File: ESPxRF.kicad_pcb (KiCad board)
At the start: 4 copper layers, 66.6 x 27.7 mm, 37 parts, among them J1 USB_C_Receptacle_USB2.0, J2 ANT, U1 NCP115ASN330T2G, U2 NRF24L01, U3 USBLC6-2SC6, U4 ESP32-S3, Y1 Crystal_GND24_Small

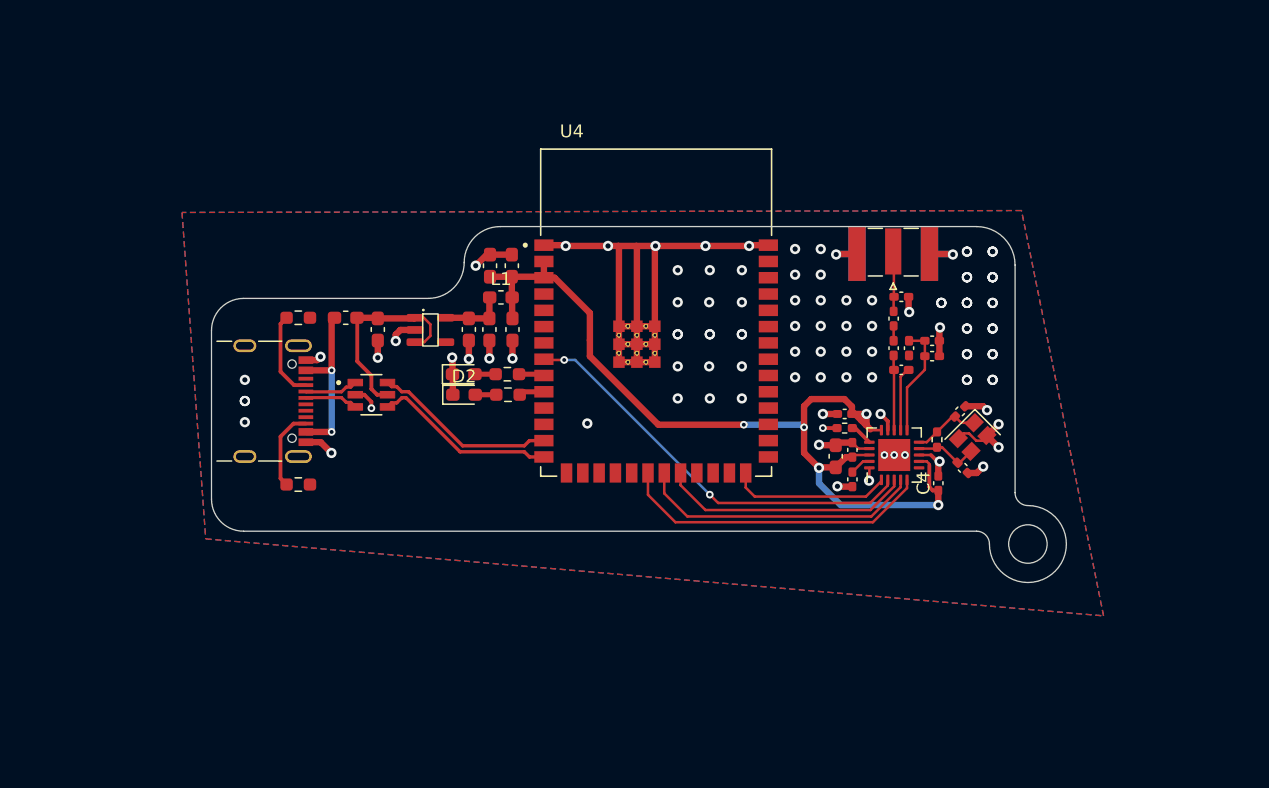
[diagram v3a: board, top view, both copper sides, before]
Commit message: made the ring sturdier and m2
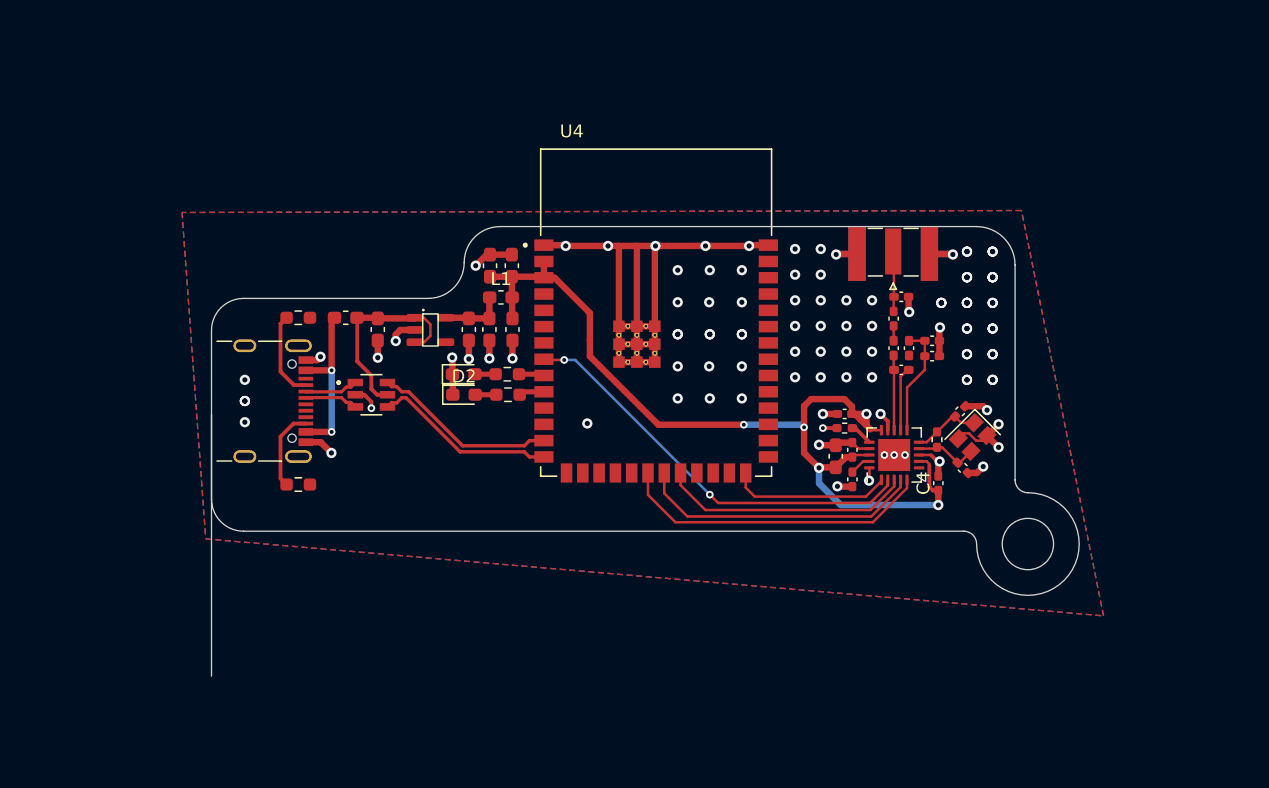
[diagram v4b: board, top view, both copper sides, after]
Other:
- board size 66.6 x 27.7 mm -> 67.6 x 35 mm
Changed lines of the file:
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@@
     )
   )
-  (gr_line (start 148.95 62.25) (end 148.95 80)
+  (gr_line (start 148.95 62.25) (end 148.95 79)
     (stroke (width 0.1) (type default)) (layer "Edge.Cuts"))
   (gr_arc (start 106 62.05) (mid 106.820101 60.070101) (end 108.8 59.25)
@@
   (gr_line (start 88.8 64.85) (end 103.2 64.85)
     (stroke (width 0.1) (type default)) (layer "Edge.Cuts"))
+  (gr_arc (start 144.95 83) (mid 145.657107 83.292893) (end 145.95 84)
+    (stroke (width 0.1) (type default)) (layer "Edge.Cuts"))
   (gr_arc (start 145.95 59.25) (mid 148.07132 60.12868) (end 148.95 62.25)
     (stroke (width 0.1) (type default)) (layer "Edge.Cuts"))
-  (gr_arc (start 145.95 83) (mid 146.657107 83.292893) (end 146.95 84)
-    (stroke (width 0.1) (type default)) (layer "Edge.Cuts"))
   (gr_line (start 108.8 59.25) (end 145.95 59.25)
     (stroke (width 0.1) (type default)) (layer "Edge.Cuts"))
-  (gr_circle (center 149.95 84) (end 151.45 84)
+  (gr_circle (center 149.95 84) (end 151.95 84)
     (stroke (width 0.1) (type default)) (fill none) (layer "Edge.Cuts"))
-  (gr_arc (start 149.95 81) (mid 152.07132 86.12132) (end 146.95 84)
-    (stroke (width 0.1) (type default)) (layer "Edge.Cuts"))
-  (gr_line (start 88.8 83) (end 145.95 83)
-    (stroke (width 0.1) (type default)) (layer "Edge.Cuts"))
-  (gr_arc (start 149.95 81) (mid 149.242893 80.707107) (end 148.95 80)
+  (gr_arc (start 149.95 80) (mid 152.778427 86.828427) (end 145.95 84)
+    (stroke (width 0.1) (type default)) (layer "Edge.Cuts"))
+  (gr_line (start 88.8 83) (end 144.95 83)
+    (stroke (width 0.1) (type default)) (layer "Edge.Cuts"))
+  (gr_arc (start 149.95 80) (mid 149.242893 79.707107) (end 148.95 79)
+    (stroke (width 0.1) (type default)) (layer "Edge.Cuts"))
+  (gr_line (start 86.3 73.925) (end 86.3 94.3)
     (stroke (width 0.1) (type default)) (layer "Edge.Cuts"))
   (gr_arc (start 88.8 83) (mid 87.032233 82.267767) (end 86.3 80.5)
@@
   (gr_text "RX" (at 102.165 71.56) (layer "F.Fab")
     (effects (font (size 1 1) (thickness 0.25) bold) (justify left bottom))
+  )
+  (dimension (type aligned) (layer "Edge.Cuts")
+    (pts (xy 86.3 84) (xy 153.95 84))
+    (height 7.999999)
+    (gr_text "67.6500 mm" (at 120.125 90.849999) (layer "Edge.Cuts")
+      (effects (font (size 1 1) (thickness 0.15)))
+    )
+    (format (prefix "") (suffix "") (units 3) (units_format 1) (precision 4))
+    (style (thickness 0.1) (arrow_length 1.27) (text_position_mode 0) (extension_height 0.58642) (extension_offset 0.5) keep_text_aligned)
+  )
+  (dimension (type aligned) (layer "Edge.Cuts")
+    (pts (xy 149.95 59.25) (xy 149.95 88))
+    (height -7.3)
+    (gr_text "28.7500 mm" (at 156.1 73.625 90) (layer "Edge.Cuts")
+      (effects (font (size 1 1) (thickness 0.15)))
+    )
+    (format (prefix "") (suffix "") (units 3) (units_format 1) (precision 4))
+    (style (thickness 0.1) (arrow_length 1.27) (text_position_mode 0) (extension_height 0.58642) (extension_offset 0.5) keep_text_aligned)
   )
   (segment (start 141.915 70.415946) (end 140.5275 71.803446) (width 0.2) (layer "F.Cu") (net 1))
@@
     (polygon
       (pts
-        (xy 152.95 84)
-        (xy 152.929715 83.651721)
-        (xy 152.869135 83.308152)
-        (xy 152.769078 82.97394)
-        (xy 152.630898 82.653602)
-        (xy 152.456463 82.351473)
-        (xy 152.248133 82.071637)
-        (xy 152.008725 81.817879)
-        (xy 151.741476 81.59363)
-        (xy 151.45 81.401924)
-        (xy 151.138239 81.245352)
-        (xy 150.81041 81.126031)
-        (xy 150.470945 81.045577)
-        (xy 150.124434 81.005076)
-        (xy 149.775566 81.005076)
-        (xy 149.429055 81.045577)
-        (xy 149.08959 81.126031)
-        (xy 148.761761 81.245352)
-        (xy 148.45 81.401924)
-        (xy 148.158524 81.59363)
-        (xy 147.891275 81.817879)
-        (xy 147.651867 82.071637)
-        (xy 147.443537 82.351473)
-        (xy 147.269102 82.653602)
-        (xy 147.130922 82.97394)
-        (xy 147.030865 83.308152)
-        (xy 146.970285 83.651721)
-        (xy 146.95 84)
-        (xy 146.970285 84.348279)
-        (xy 147.030865 84.691848)
-        (xy 147.130922 85.02606)
-        (xy 147.269102 85.346398)
-        (xy 147.443537 85.648527)
-        (xy 147.651867 85.928363)
-        (xy 147.891275 86.182121)
-        (xy 148.158524 86.40637)
-        (xy 148.45 86.598076)
-        (xy 148.761761 86.754648)
-        (xy 149.08959 86.873969)
-        (xy 149.429055 86.954423)
-        (xy 149.775566 86.994924)
-        (xy 150.124434 86.994924)
-        (xy 150.470945 86.954423)
-        (xy 150.81041 86.873969)
-        (xy 151.138239 86.754648)
-        (xy 151.45 86.598076)
-        (xy 151.741476 86.40637)
-        (xy 152.008725 86.182121)
-        (xy 152.248133 85.928363)
-        (xy 152.456463 85.648527)
-        (xy 152.630898 85.346398)
-        (xy 152.769078 85.02606)
-        (xy 152.869135 84.691848)
-        (xy 152.929715 84.348279)
-        (xy 152.95 84)
+        (xy 153.95 84)
+        (xy 153.930739 83.607931)
+        (xy 153.873141 83.219639)
+        (xy 153.777761 82.838861)
+        (xy 153.645518 82.469266)
+        (xy 153.477685 82.114413)
+        (xy 153.275878 81.777719)
+        (xy 153.042042 81.462427)
+        (xy 152.778427 81.171573)
+        (xy 152.487573 80.907958)
+        (xy 152.172281 80.674122)
+        (xy 151.835587 80.472315)
+        (xy 151.480734 80.304482)
+        (xy 151.111139 80.172239)
+        (xy 150.730361 80.076859)
+        (xy 150.342069 80.019261)
+        (xy 149.95 80)
+        (xy 149.557931 80.019261)
+        (xy 149.169639 80.076859)
+        (xy 148.788861 80.172239)
+        (xy 148.419266 80.304482)
+        (xy 148.064413 80.472315)
+        (xy 147.727719 80.674122)
+        (xy 147.412427 80.907958)
+        (xy 147.121573 81.171573)
+        (xy 146.857958 81.462427)
+        (xy 146.624122 81.777719)
+        (xy 146.422315 82.114413)
+        (xy 146.254482 82.469266)
+        (xy 146.122239 82.838861)
+        (xy 146.026859 83.219639)
+        (xy 145.969261 83.607931)
+        (xy 145.95 84)
+        (xy 145.969261 84.392069)
+        (xy 146.026859 84.780361)
+        (xy 146.122239 85.161139)
+        (xy 146.254482 85.530734)
+        (xy 146.422315 85.885587)
+        (xy 146.624122 86.222281)
+        (xy 146.857958 86.537573)
+        (xy 147.121573 86.828427)
+        (xy 147.412427 87.092042)
+        (xy 147.727719 87.325878)
+        (xy 148.064413 87.527685)
+        (xy 148.419266 87.695518)
+        (xy 148.788861 87.827761)
+        (xy 149.169639 87.923141)
+        (xy 149.557931 87.980739)
+        (xy 149.95 88)
+        (xy 150.342069 87.980739)
+        (xy 150.730361 87.923141)
+        (xy 151.111139 87.827761)
+        (xy 151.480734 87.695518)
+        (xy 151.835587 87.527685)
+        (xy 152.172281 87.325878)
+        (xy 152.487573 87.092042)
+        (xy 152.778427 86.828427)
+        (xy 153.042042 86.537573)
+        (xy 153.275878 86.222281)
+        (xy 153.477685 85.885587)
+        (xy 153.645518 85.530734)
+        (xy 153.777761 85.161139)
+        (xy 153.873141 84.780361)
+        (xy 153.930739 84.392069)
+        (xy 153.95 84)
       )
     )

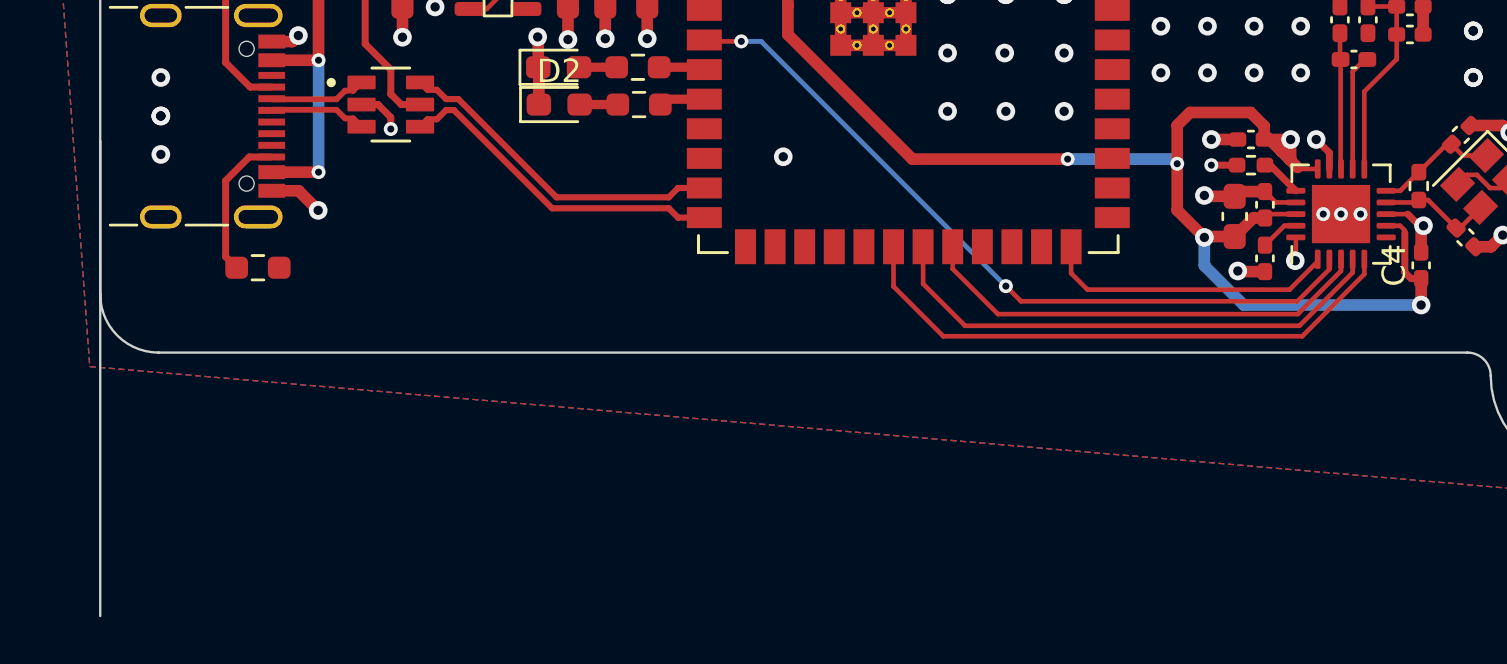
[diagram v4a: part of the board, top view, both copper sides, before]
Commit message: added pcb size measurements
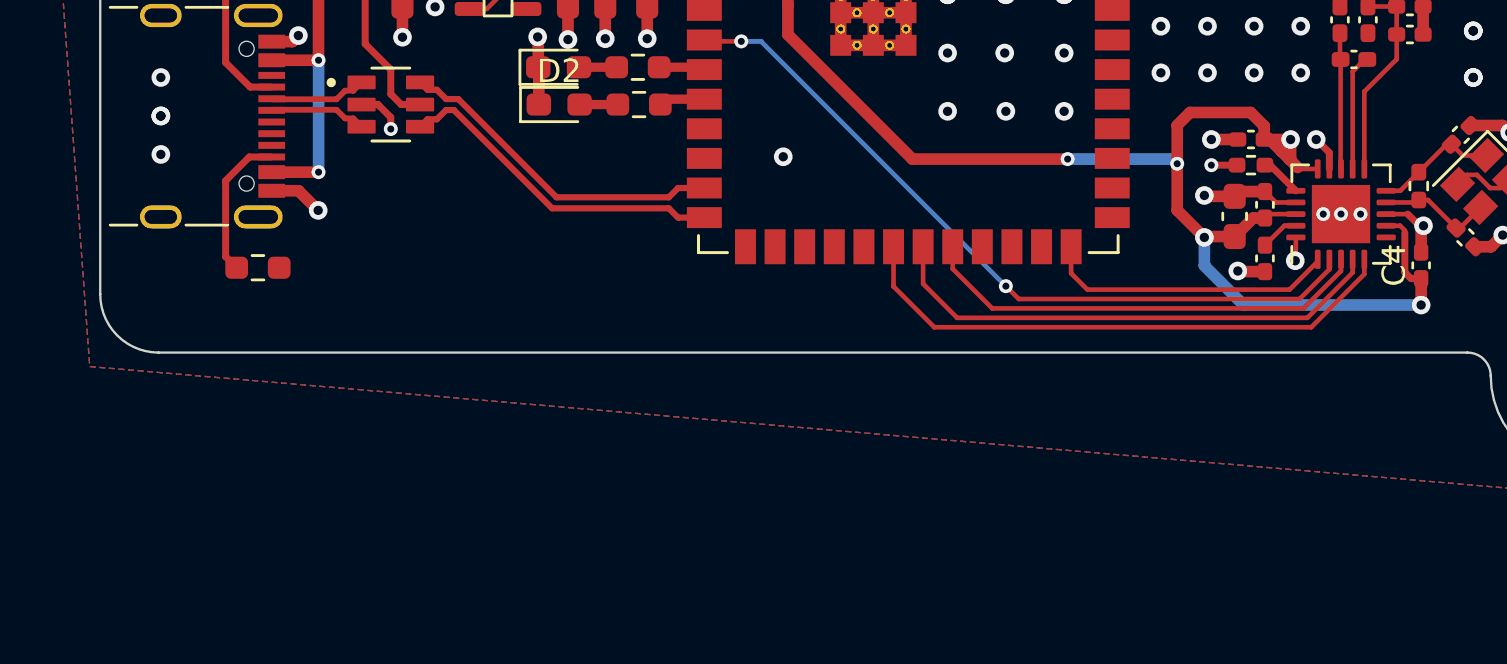
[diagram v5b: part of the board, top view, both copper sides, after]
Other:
- board size 67.6 x 35 mm -> 67.6 x 28.7 mm
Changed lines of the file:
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@@
   (gr_arc (start 149.95 80) (mid 149.242893 79.707107) (end 148.95 79)
-    (stroke (width 0.1) (type default)) (layer "Edge.Cuts"))
-  (gr_line (start 86.3 73.925) (end 86.3 94.3)
     (stroke (width 0.1) (type default)) (layer "Edge.Cuts"))
   (gr_arc (start 88.8 83) (mid 87.032233 82.267767) (end 86.3 80.5)
@@
   )
   (dimension (type aligned) (layer "Edge.Cuts")
-    (pts (xy 86.3 84) (xy 153.95 84))
-    (height 7.999999)
-    (gr_text "67.6500 mm" (at 120.125 90.849999) (layer "Edge.Cuts")
+    (pts (xy 149.95 59.25) (xy 149.95 88))
+    (height -7.7)
+    (gr_text "28.7500 mm" (at 156.5 73.625 90) (layer "Edge.Cuts")
       (effects (font (size 1 1) (thickness 0.15)))
     )
@@
   )
   (dimension (type aligned) (layer "Edge.Cuts")
-    (pts (xy 149.95 59.25) (xy 149.95 88))
-    (height -7.3)
-    (gr_text "28.7500 mm" (at 156.1 73.625 90) (layer "Edge.Cuts")
+    (pts (xy 86.3 84) (xy 153.95 84))
+    (height 7.999999)
+    (gr_text "67.6500 mm" (at 120.125 90.849999) (layer "Edge.Cuts")
       (effects (font (size 1 1) (thickness 0.15)))
     )
@@
   (segment (start 138.5275 78.9975) (end 138.5275 79.091975) (width 0.2) (layer "F.Cu") (net 9))
   (segment (start 128.65 80.3) (end 127.95 79.6) (width 0.2) (layer "F.Cu") (net 9))
+  (segment (start 137.751478 80.7032) (end 125.7032 80.7032) (width 0.2) (layer "F.Cu") (net 10))
+  (segment (start 112.275 69.65) (end 112.215 69.59) (width 0.2) (layer "F.Cu") (net 10))
+  (segment (start 139.0275 79.427178) (end 137.751478 80.7032) (width 0.2) (layer "F.Cu") (net 10))
+  (segment (start 125.7032 80.7032) (end 125.15 80.15) (width 0.2) (layer "F.Cu") (net 10))
+  (segment (start 113.8 69.65) (end 112.275 69.65) (width 0.2) (layer "F.Cu") (net 10))
   (segment (start 139.0275 78.9975) (end 139.0275 79.427178) (width 0.2) (layer "F.Cu") (net 10))
-  (segment (start 112.275 69.65) (end 112.215 69.59) (width 0.2) (layer "F.Cu") (net 10))
-  (segment (start 139.0275 79.427178) (end 137.654678 80.8) (width 0.2) (layer "F.Cu") (net 10))
-  (segment (start 125.8 80.8) (end 125.15 80.15) (width 0.2) (layer "F.Cu") (net 10))
-  (segment (start 113.8 69.65) (end 112.275 69.65) (width 0.2) (layer "F.Cu") (net 10))
-  (segment (start 137.654678 80.8) (end 125.8 80.8) (width 0.2) (layer "F.Cu") (net 10))
   (via (at 125.15 80.15) (size 0.6) (drill 0.3) (layers "F.Cu" "B.Cu") (net 10))
   (via (at 113.8 69.65) (size 0.6) (drill 0.3) (layers "F.Cu" "B.Cu") (net 10))
   (segment (start 114.65 69.65) (end 113.8 69.65) (width 0.2) (layer "B.Cu") (net 10))
   (segment (start 125.15 80.15) (end 114.65 69.65) (width 0.2) (layer "B.Cu") (net 10))
-  (segment (start 137.674888 81.35) (end 124.81 81.35) (width 0.2) (layer "F.Cu") (net 11))
+  (segment (start 122.87 79.41) (end 122.87 78.46) (width 0.2) (layer "F.Cu") (net 11))
   (segment (start 139.5275 78.9975) (end 139.5275 79.497388) (width 0.2) (layer "F.Cu") (net 11))
-  (segment (start 139.5275 79.497388) (end 137.674888 81.35) (width 0.2) (layer "F.Cu") (net 11))
-  (segment (start 124.81 81.35) (end 122.87 79.41) (width 0.2) (layer "F.Cu") (net 11))
-  (segment (start 122.87 79.41) (end 122.87 78.46) (width 0.2) (layer "F.Cu") (net 11))
-  (segment (start 140.0275 79.567598) (end 137.745098 81.85) (width 0.2) (layer "F.Cu") (net 12))
-  (segment (start 123.4 81.85) (end 121.6 80.05) (width 0.2) (layer "F.Cu") (net 12))
+  (segment (start 124.5664 81.1064) (end 122.87 79.41) (width 0.2) (layer "F.Cu") (net 11))
+  (segment (start 137.918488 81.1064) (end 124.5664 81.1064) (width 0.2) (layer "F.Cu") (net 11))
+  (segment (start 139.5275 79.497388) (end 137.918488 81.1064) (width 0.2) (layer "F.Cu") (net 11))
   (segment (start 140.0275 78.9975) (end 140.0275 79.567598) (width 0.2) (layer "F.Cu") (net 12))
-  (segment (start 137.745098 81.85) (end 123.4 81.85) (width 0.2) (layer "F.Cu") (net 12))
+  (segment (start 138.085498 81.5096) (end 123.0596 81.5096) (width 0.2) (layer "F.Cu") (net 12))
+  (segment (start 123.0596 81.5096) (end 121.6 80.05) (width 0.2) (layer "F.Cu") (net 12))
+  (segment (start 140.0275 79.567598) (end 138.085498 81.5096) (width 0.2) (layer "F.Cu") (net 12))
   (segment (start 121.6 80.05) (end 121.6 78.46) (width 0.2) (layer "F.Cu") (net 12))
+  (segment (start 138.252508 81.9128) (end 122.07939 81.9128) (width 0.2) (layer "F.Cu") (net 13))
   (segment (start 120.33 80.16341) (end 120.33 78.46) (width 0.2) (layer "F.Cu") (net 13))
-  (segment (start 122.46659 82.3) (end 120.33 80.16341) (width 0.2) (layer "F.Cu") (net 13))
+  (segment (start 122.07939 81.9128) (end 120.33 80.16341) (width 0.2) (layer "F.Cu") (net 13))
+  (segment (start 140.5275 79.637808) (end 138.252508 81.9128) (width 0.2) (layer "F.Cu") (net 13))
   (segment (start 140.5275 78.9975) (end 140.5275 79.637808) (width 0.2) (layer "F.Cu") (net 13))
-  (segment (start 140.5275 79.637808) (end 137.865308 82.3) (width 0.2) (layer "F.Cu") (net 13))
-  (segment (start 137.865308 82.3) (end 122.46659 82.3) (width 0.2) (layer "F.Cu") (net 13))
   (segment (start 107.965 66.3725) (end 107.965 64.7975) (width 0.5) (layer "F.Cu") (net 15))
   (segment (start 107.915 66.3225) (end 107.965 66.3725) (width 0.5) (layer "F.Cu") (net 15))

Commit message: added GND plane in two inner layers
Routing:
- added copper zone on In1.Cu, net GND
- added copper zone on In2.Cu, net GND
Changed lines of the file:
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@@
     (pad "6" smd roundrect (at 1.255 -0.95) (size 1.21 0.59) (layers "F.Cu" "F.Paste" "F.Mask") (roundrect_rratio 0.07)
       (net 34 "USB_D-") (pintype "bidirectional"))
-    (model "C:/Program Files/KiCad/6.0/share/kicad/3dmodels/Diode_SMD.3dshapes/USBLC6-2SC6.STEP"
+    (model "${KIPRJMOD}/KicadLibs/USBLC6-2SC6/USBLC6-2SC6.STEP"
       (offset (xyz 0 0 1))
       (scale (xyz 1 1 1))
@@
     (pad "2" smd rect (at 2.825 0 180) (size 1.35 4.2) (layers "B.Cu" "B.Paste" "B.Mask")
       (net 22 "GND") (pinfunction "Ext") (pintype "passive"))
-    (model "C:/Program Files/KiCad/6.0/share/kicad/3dmodels/Connector_Coaxial.3dshapes/SMA Connector Edge Mount.step"
+    (model "${KIPRJMOD}/KicadLibs/Antenna/SMA Connector Edge Mount.step"
       (offset (xyz 0 -2.5 -1))
       (scale (xyz 1 1 1))
@@
   (segment (start 110.5575 72.13) (end 110.3275 72.36) (width 0.4) (layer "F.Cu") (net 58))
   (segment (start 112.215 72.13) (end 110.5575 72.13) (width 0.4) (layer "F.Cu") (net 58))
-  (zone (net 22) (net_name "GND") (layers "F&B.Cu") (hatch edge 0.5)
+  (zone (net 22) (net_name "GND") (layers "F.Cu" "In1.Cu" "In2.Cu" "B.Cu") (hatch edge 0.5)
     (connect_pads (clearance 0.5))
     (min_thickness 0.25) (filled_areas_thickness no)
@@
         (xy 153.873141 84.780361)
         (xy 153.930739 84.392069)
-        (xy 153.95 84)
       )
     )
